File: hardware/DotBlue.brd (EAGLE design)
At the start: 24 x 24 mm, 15 parts, among them IC1 CP2101, J3 USB-MICROB, U1 RFD77101, X3 S4B-ZR

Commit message: Add RGB connections
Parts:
- moved LED1 12.3 mm to (22.3, 8.53)
- moved R1 11.8 mm to (21.6, 20.3), turned to 270 degrees
- moved C3 0.34 mm to (10.4, 6.63)
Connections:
- net LED_BLUE: now also U1.39
- net LED_GREEN: now also U1.40
- net LED_RED: now also U1.38
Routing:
- net SDA: track 16.1 -> 28.6 mm
- net N$4: track 14.2 -> 22.0 mm, vias 0 -> 2
- net N$2: track 20.6 -> 28.3 mm, vias 0 -> 3
- net SCL: track 9.42 -> 15.9 mm
- net N$1: track 11.2 -> 17.2 mm, vias 0 -> 2
- net +5V: track 46.2 -> 49.3 mm, vias 2 -> 3
- net LED_GREEN: track 0.00 -> 2.84 mm
- net LED_BLUE: track 0.00 -> 2.69 mm
- net RESET: track 3.63 -> 6.31 mm
- net LED_RED: track 0.00 -> 2.65 mm
- net AIN5: track 7.24 -> 9.52 mm
- net N$3: track 8.01 -> 7.16 mm
- net +3V3: track 56.8 -> 57.5 mm, vias 3 -> 4
- net N$15: track 14.0 -> 13.3 mm, vias 0 -> 2
- net USB_D+: track 10.8 -> 10.2 mm, vias 2 -> 0
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
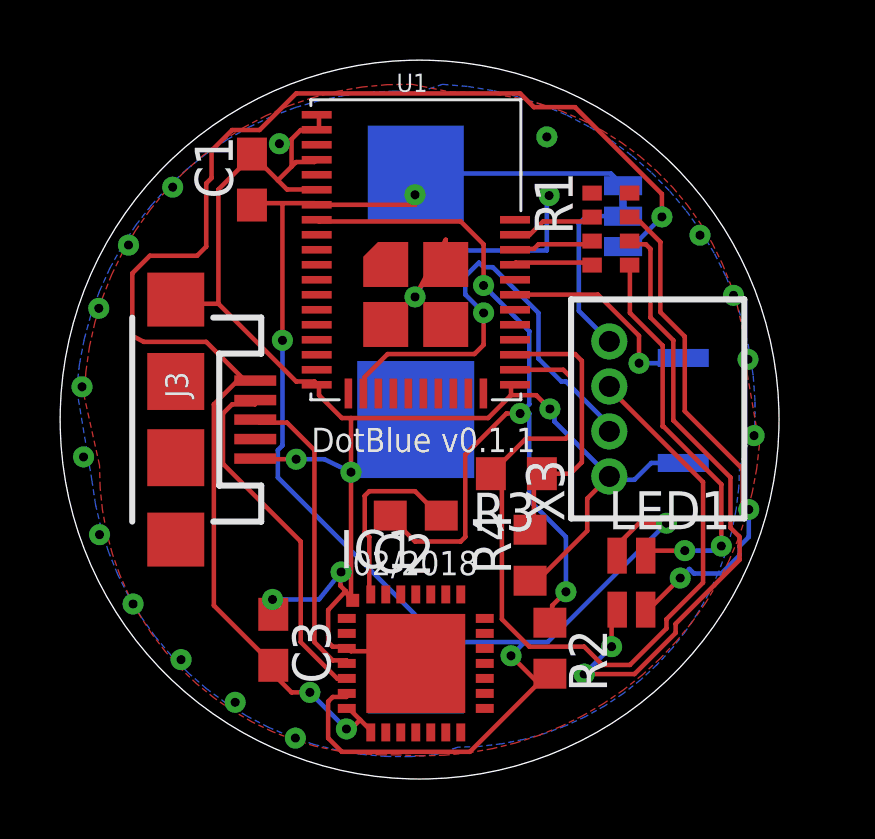
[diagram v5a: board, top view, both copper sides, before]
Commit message: Add UART connections
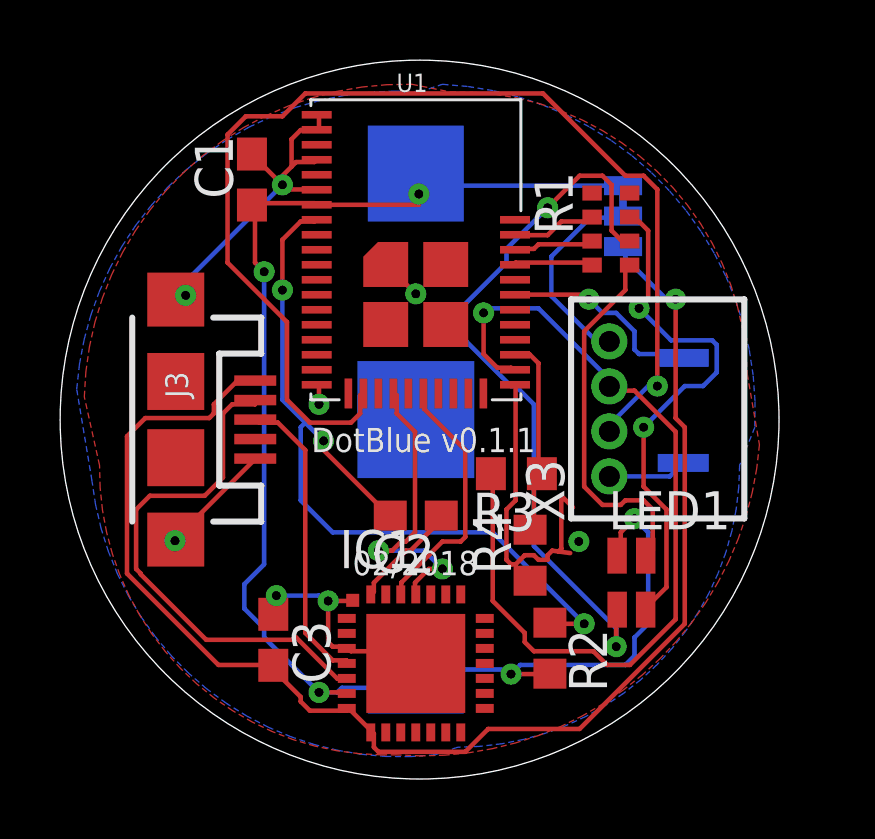
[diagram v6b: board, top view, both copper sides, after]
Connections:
- net RXD: now also IC1.26
- net TXD: now also IC1.25
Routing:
- net GND: track 67.3 -> 39.7 mm, vias 23 -> 8
- net SCL: track 15.9 -> 38.6 mm
- net TXD: track 0.00 -> 10.3 mm, vias 0 -> 2
- net RXD: track 0.00 -> 8.51 mm
- net +3V3: track 57.5 -> 51.6 mm, vias 4 -> 5
- net USB_D-: track 12.1 -> 17.4 mm
- net AIN5: track 9.52 -> 6.75 mm
- net RESET: track 6.31 -> 3.72 mm
- net N$4: track 22.0 -> 24.5 mm
- net +5V: track 49.3 -> 46.8 mm, vias 3 -> 1
- net N$2: track 28.3 -> 27.1 mm
- net N$5: track 5.92 -> 6.82 mm
- net N$15: track 13.3 -> 12.4 mm, vias 2 -> 0
- net SDA: track 28.6 -> 29.3 mm, vias 0 -> 1

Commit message: Resolidify GND
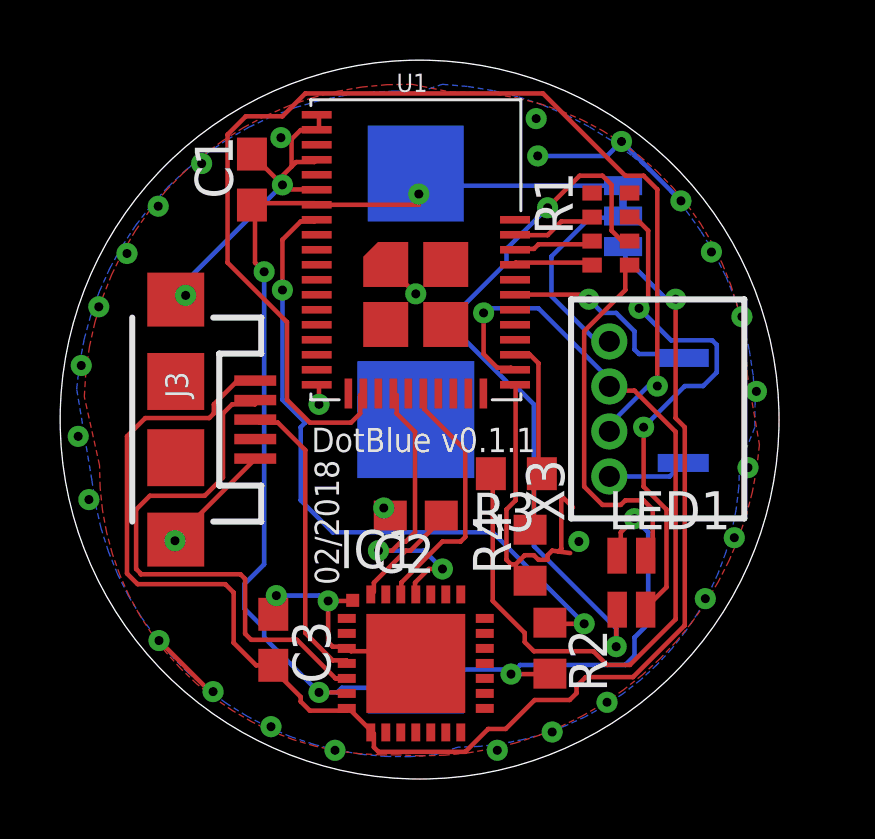
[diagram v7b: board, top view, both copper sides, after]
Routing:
- net GND: track 39.7 -> 48.0 mm, vias 8 -> 33
- net N$2: track 27.1 -> 24.2 mm
- net USB_D-: track 17.4 -> 18.7 mm
- net +5V: track 46.8 -> 47.9 mm
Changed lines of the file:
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@@
 <rectangle x1="12.573" y1="20.955" x2="18.669" y2="24.638" layer="42"/>
 <text x="19.099096875" y="13.6985625" size="0.8128" layer="21" rot="R180">DotBlue v0.1.1</text>
-<text x="13.006503125" y="8.7804375" size="0.8128" layer="21">02/2018</text>
+<text x="12.5555625" y="8.459903125" size="0.8128" layer="21" rot="R90">02/2018</text>
 <dimension x1="3.258853125" y1="13.957228125" x2="27.221146875" y2="13.982771875" x3="15.2146" y3="37.7952" textsize="1.778" layer="47" dtype="diameter"/>
 </plain>
@@
 <wire x1="19.9644" y1="9.667271875" x2="19.869890625" y2="9.5727625" width="0.1524" layer="1"/>
 <via x="20.5486" y="9.906" extent="1-16" drill="0.3"/>
-<wire x1="16.111" y1="17.14" x2="18.421" y2="15.13" width="0" layer="19" extent="1-1"/>
-<wire x1="7.112" y1="9.97" x2="7.0866" y2="9.9314" width="0" layer="19" extent="1-1"/>
+<via x="10.6172" y="23.368" extent="1-16" drill="0.3"/>
+<via x="7.9756" y="22.5044" extent="1-16" drill="0.3"/>
+<via x="6.5278" y="21.082" extent="1-16" drill="0.3"/>
+<via x="5.4864" y="19.5072" extent="1-16" drill="0.3"/>
+<via x="4.5466" y="17.7292" extent="1-16" drill="0.3"/>
+<via x="3.9624" y="15.7734" extent="1-16" drill="0.3"/>
+<via x="3.8608" y="13.4112" extent="1-16" drill="0.3"/>
+<via x="4.2164" y="11.303" extent="1-16" drill="0.3"/>
+<via x="6.5532" y="6.604" extent="1-16" drill="0.3"/>
+<via x="8.3566" y="4.9022" extent="1-16" drill="0.3"/>
+<via x="10.287" y="3.7338" extent="1-16" drill="0.3"/>
+<via x="12.4206" y="2.9464" extent="1-16" drill="0.3"/>
+<via x="17.8308" y="2.9464" extent="1-16" drill="0.3"/>
+<via x="19.6596" y="3.556" extent="1-16" drill="0.3"/>
+<via x="21.4884" y="4.5466" extent="1-16" drill="0.3"/>
+<wire x1="6.5532" y1="6.604" x2="8.255" y2="4.9022" width="0.1524" layer="1"/>
+<wire x1="8.255" y1="4.9022" x2="8.3566" y2="4.9022" width="0.1524" layer="1"/>
+<via x="24.765" y="8.001" extent="1-16" drill="0.3"/>
+<via x="25.7302" y="10.033" extent="1-16" drill="0.3"/>
+<via x="26.1874" y="12.3698" extent="1-16" drill="0.3"/>
+<via x="26.4668" y="14.9098" extent="1-16" drill="0.3"/>
+<via x="25.9842" y="17.399" extent="1-16" drill="0.3"/>
+<via x="24.9682" y="19.558" extent="1-16" drill="0.3"/>
+<via x="23.9522" y="21.2598" extent="1-16" drill="0.3"/>
+<via x="21.971" y="23.241" extent="1-16" drill="0.3"/>
+<via x="19.1262" y="24.003" extent="1-16" drill="0.3"/>
+<via x="19.177" y="22.7584" extent="1-16" drill="0.3"/>
+<wire x1="21.971" y1="23.241" x2="21.4884" y2="22.7584" width="0.1524" layer="16"/>
+<wire x1="21.4884" y1="22.7584" x2="19.177" y2="22.7584" width="0.1524" layer="16"/>
+<wire x1="21.971" y1="23.241" x2="23.9522" y2="21.2598" width="0.1524" layer="16"/>
+<wire x1="7.0866" y1="9.9314" x2="7.112" y2="9.97" width="0" layer="19" extent="1-1"/>
+<wire x1="18.421" y1="15.13" x2="16.111" y2="17.14" width="0" layer="19" extent="1-1"/>
 </signal>
 <signal name="+5V">
@@
 <wire x1="23.7744" y1="14.0208" x2="23.7744" y2="17.9832" width="0.1524" layer="1"/>
 <wire x1="24.0792" y1="13.716" x2="23.7744" y2="14.0208" width="0.1524" layer="1"/>
-<wire x1="24.0792" y1="7.1628" x2="24.0792" y2="13.716" width="0.1524" layer="1"/>
-<wire x1="20.574" y1="3.6576" x2="24.0792" y2="7.1628" width="0.1524" layer="1"/>
-<wire x1="17.526" y1="3.6576" x2="20.574" y2="3.6576" width="0.1524" layer="1"/>
+<wire x1="24.0792" y1="7.112" x2="24.0792" y2="13.716" width="0.1524" layer="1"/>
 <wire x1="16.764" y1="2.8956" x2="17.526" y2="3.6576" width="0.1524" layer="1"/>
 <wire x1="13.8684" y1="2.8956" x2="16.764" y2="2.8956" width="0.1524" layer="1"/>
@@
 <wire x1="5.4864" y1="13.4112" x2="6.096" y2="14.0208" width="0.1524" layer="1"/>
 <wire x1="5.4864" y1="8.8392" x2="5.4864" y2="13.4112" width="0.1524" layer="1"/>
-<wire x1="8.5344" y1="5.7912" x2="5.4864" y2="8.8392" width="0.1524" layer="1"/>
-<wire x1="10.3632" y1="5.7912" x2="8.5344" y2="5.7912" width="0.1524" layer="1"/>
 <wire x1="9.7536" y1="15.24" x2="9.762" y2="15.27" width="0.1524" layer="1"/>
 <wire x1="10.3632" y1="5.7912" x2="10.3632" y2="5.7794" width="0.1524" layer="1"/>
 <via x="23.7744" y="17.9832" extent="1-16" drill="0.3"/>
+<wire x1="24.0792" y1="7.112" x2="22.352" y2="5.3848" width="0.1524" layer="1"/>
+<wire x1="22.352" y1="5.3848" x2="20.7772" y2="5.3848" width="0.1524" layer="1"/>
+<wire x1="20.7772" y1="5.3848" x2="20.4724" y2="5.08" width="0.1524" layer="1"/>
+<wire x1="20.4724" y1="5.08" x2="20.4724" y2="4.8514" width="0.1524" layer="1"/>
+<wire x1="20.4724" y1="4.8514" x2="20.2438" y2="4.6228" width="0.1524" layer="1"/>
+<wire x1="19.0754" y1="4.6228" x2="18.1102" y2="3.6576" width="0.1524" layer="1"/>
+<wire x1="18.1102" y1="3.6576" x2="17.526" y2="3.6576" width="0.1524" layer="1"/>
+<wire x1="5.4864" y1="8.8392" x2="5.842" y2="8.4836" width="0.1524" layer="1"/>
+<wire x1="5.842" y1="8.4836" x2="8.763" y2="8.4836" width="0.1524" layer="1"/>
+<wire x1="8.763" y1="8.4836" x2="9.0424" y2="8.2042" width="0.1524" layer="1"/>
+<wire x1="9.0424" y1="8.2042" x2="9.0424" y2="6.5278" width="0.1524" layer="1"/>
+<wire x1="9.0424" y1="6.5278" x2="9.7908" y2="5.7794" width="0.1524" layer="1"/>
+<wire x1="9.7908" y1="5.7794" x2="10.3632" y2="5.7794" width="0.1524" layer="1"/>
+<wire x1="20.2438" y1="4.6228" x2="19.0754" y2="4.6228" width="0.1524" layer="1"/>
 </signal>
 <signal name="USB_D-">
@@
 <contactref element="IC1" pad="5"/>
 <wire x1="12.4968" y1="5.334" x2="12.8016" y2="5.334" width="0.1524" layer="1"/>
-<wire x1="11.1252" y1="6.7056" x2="12.4968" y2="5.334" width="0.1524" layer="1"/>
 <wire x1="5.7912" y1="8.9916" x2="5.9436" y2="8.8392" width="0.1524" layer="1"/>
 <wire x1="5.7912" y1="10.9728" x2="5.7912" y2="8.9916" width="0.1524" layer="1"/>
@@
 <wire x1="9.7536" y1="14.478" x2="9.762" y2="14.62" width="0.1524" layer="1"/>
 <wire x1="5.9436" y1="8.8392" x2="5.9436" y2="8.8138" width="0.1524" layer="1"/>
-<wire x1="5.9436" y1="8.8138" x2="8.128" y2="6.6294" width="0.1524" layer="1"/>
-<wire x1="8.128" y1="6.6294" x2="11.049" y2="6.6294" width="0.1524" layer="1"/>
-<wire x1="11.049" y1="6.6294" x2="11.1252" y2="6.7056" width="0.1524" layer="1"/>
+<wire x1="5.9436" y1="8.8138" x2="9.271" y2="8.8138" width="0.1524" layer="1"/>
+<wire x1="9.271" y1="8.8138" x2="9.4234" y2="8.6614" width="0.1524" layer="1"/>
+<wire x1="9.4234" y1="8.6614" x2="9.4234" y2="6.8326" width="0.1524" layer="1"/>
+<wire x1="9.4234" y1="6.8326" x2="9.6266" y2="6.6294" width="0.1524" layer="1"/>
+<wire x1="9.6266" y1="6.6294" x2="11.1506" y2="6.6294" width="0.1524" layer="1"/>
+<wire x1="11.1506" y1="6.6294" x2="12.438" y2="5.342" width="0.1524" layer="1"/>
+<wire x1="12.438" y1="5.342" x2="12.813" y2="5.342" width="0.1524" layer="1"/>
 </signal>
 <signal name="USB_D+">
@@
 <wire x1="16.002" y1="8.9916" x2="15.5448" y2="8.9916" width="0.1524" layer="1"/>
 <wire x1="15.3924" y1="9.6012" x2="16.002" y2="8.9916" width="0.1524" layer="16"/>
-<wire x1="13.8684" y1="9.6012" x2="15.3924" y2="9.6012" width="0.1524" layer="16"/>
 <wire x1="14.3256" y1="9.6012" x2="13.8684" y2="9.6012" width="0.1524" layer="1"/>
 <wire x1="14.6304" y1="9.906" x2="14.3256" y2="9.6012" width="0.1524" layer="1"/>
@@
 <wire x1="14.478" y1="14.7828" x2="14.366" y2="14.84" width="0.1524" layer="1"/>
 <via x="16.002" y="8.9916" extent="1-16" drill="0.3"/>
+<wire x1="13.8684" y1="9.6012" x2="15.3924" y2="9.6012" width="0.1524" layer="16"/>
 <via x="13.8684" y="9.6012" extent="1-16" drill="0.3"/>
 </signal>
@@
 <wire x1="10.668" y1="18.288" x2="10.668" y2="19.9644" width="0.1524" layer="1"/>
 <wire x1="10.668" y1="14.6304" x2="10.668" y2="18.288" width="0.1524" layer="16"/>
-<wire x1="12.0396" y1="13.2588" x2="11.43" y2="13.8684" width="0.1524" layer="16"/>
 <wire x1="11.43" y1="13.8684" x2="10.668" y2="14.6304" width="0.1524" layer="16"/>
-<wire x1="12.0396" y1="12.954" x2="12.0396" y2="13.2588" width="0.1524" layer="1"/>
-<wire x1="14.1732" y1="10.8204" x2="12.0396" y2="12.954" width="0.1524" layer="1"/>
 <wire x1="11.7348" y1="20.574" x2="11.811" y2="20.63" width="0.1524" layer="1"/>
 <wire x1="14.1732" y1="10.8204" x2="14.263" y2="10.7696" width="0.1524" layer="1"/>
 <wire x1="20.7264" y1="7.1628" x2="19.6596" y2="7.1628" width="0.1524" layer="1"/>
 <wire x1="17.6784" y1="10.2108" x2="20.7264" y2="7.1628" width="0.1524" layer="16"/>
-<wire x1="12.3444" y1="10.2108" x2="17.6784" y2="10.2108" width="0.1524" layer="16"/>
+<wire x1="12.3444" y1="10.2108" x2="13.8938" y2="10.2108" width="0.1524" layer="16"/>
+<wire x1="13.8938" y1="10.2108" x2="17.6784" y2="10.2108" width="0.1524" layer="16"/>
 <wire x1="11.2776" y1="11.2776" x2="12.3444" y2="10.2108" width="0.1524" layer="16"/>
 <wire x1="11.2776" y1="13.716" x2="11.2776" y2="11.2776" width="0.1524" layer="16"/>
@@
 <wire x1="19.6596" y1="7.1628" x2="19.5834" y2="7.2" width="0.1524" layer="1"/>
 <via x="10.668" y="18.288" extent="1-16" drill="0.3"/>
-<via x="12.0396" y="13.2588" extent="1-16" drill="0.3"/>
 <via x="20.7264" y="7.1628" extent="1-16" drill="0.3"/>
+<wire x1="14.1732" y1="10.8204" x2="14.0462" y2="10.8204" width="0.1524" layer="1"/>
+<wire x1="14.0462" y1="10.8204" x2="14.0462" y2="11.0236" width="0.1524" layer="1"/>
+<via x="14.0462" y="11.0236" extent="1-16" drill="0.3"/>
+<wire x1="14.0462" y1="11.0236" x2="13.8938" y2="11.0236" width="0.1524" layer="16"/>
+<wire x1="13.8938" y1="11.0236" x2="13.8938" y2="10.2108" width="0.1524" layer="16"/>
 </signal>
 <signal name="RESET">
